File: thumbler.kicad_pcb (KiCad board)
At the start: 2 copper layers, 255 parts, among them J1 USB_B_Micro, J2 Conn_01x04, J3 Conn_01x04, J4 DIN-5_180degree, J5 Conn_01x04, J6 DIN-5_180degree, J7 Conn_01x04, J8 USB_B_Micro, SW1 SW_Push, SW2 SW_DIP_x05, SW3 SW_Push, SW4 SW_DIP_x05, U1 STM32F072C8Tx, U2 MCP1700-3302E_SOT89, U3 MCP1700-3302E_SOT89, U4 STM32F072C8Tx, X1 ENCODER_ANO

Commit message: revised layout basically done, minus thumbs
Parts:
- removed D37, D38, D39, D40, D41, D42, D43, D44, D46, D47, D48, D49, D50, D56, D57, D58, D59, D60, D61, D62, D63, D64, D65, D67, D68, D69, D70, D71, D72, D73, D74, D75: 1N4148, Diode_THT:D_DO-35_SOD27_P7.62mm_Horizontal
- removed S36, S37, S38, S39, S40, S41, S42, S43, S47, S48, S49, S50, S51, S52, S53, S54, S55, S56, S57, S58, S59, S60, S61, S62, S63, S64, S65, S66, S67, S68, S69, S70: Kailh_Hotplug, keyswitches:Kailh_socket_MX_platemount
- added D36: 1N4148, Diode_THT:D_DO-35_SOD27_P7.62mm_Horizontal, F.Cu at (467.1, 256.4)
- added D36: 1N4148, Diode_THT:D_DO-35_SOD27_P7.62mm_Horizontal, F.Cu at (429.0, 246.9)
- added D36: 1N4148, Diode_THT:D_DO-35_SOD27_P7.62mm_Horizontal, F.Cu at (410.0, 236.9)
- added D36: 1N4148, Diode_THT:D_DO-35_SOD27_P7.62mm_Horizontal, F.Cu at (390.9, 234.9)
- added D36: 1N4148, Diode_THT:D_DO-35_SOD27_P7.62mm_Horizontal, F.Cu at (371.9, 238.9)
- added D36: 1N4148, Diode_THT:D_DO-35_SOD27_P7.62mm_Horizontal, F.Cu at (352.8, 242.9)
- added D36: 1N4148, Diode_THT:D_DO-35_SOD27_P7.62mm_Horizontal, F.Cu at (467.1, 208.8)
- added D36: 1N4148, Diode_THT:D_DO-35_SOD27_P7.62mm_Horizontal, F.Cu at (448.1, 208.8)
- added D36: 1N4148, Diode_THT:D_DO-35_SOD27_P7.62mm_Horizontal, F.Cu at (429.0, 227.8)
- added D36: 1N4148, Diode_THT:D_DO-35_SOD27_P7.62mm_Horizontal, F.Cu at (410.0, 217.8)
- added D36: 1N4148, Diode_THT:D_DO-35_SOD27_P7.62mm_Horizontal, F.Cu at (390.9, 215.8)
- added D36: 1N4148, Diode_THT:D_DO-35_SOD27_P7.62mm_Horizontal, F.Cu at (448.1, 246.9)
- added D36: 1N4148, Diode_THT:D_DO-35_SOD27_P7.62mm_Horizontal, F.Cu at (371.9, 219.8)
- added D36: 1N4148, Diode_THT:D_DO-35_SOD27_P7.62mm_Horizontal, F.Cu at (352.8, 223.8)
- added D36: 1N4148, Diode_THT:D_DO-35_SOD27_P7.62mm_Horizontal, F.Cu at (467.1, 189.7)
- added D36: 1N4148, Diode_THT:D_DO-35_SOD27_P7.62mm_Horizontal, F.Cu at (448.1, 189.7)
- added D36: 1N4148, Diode_THT:D_DO-35_SOD27_P7.62mm_Horizontal, F.Cu at (429.0, 208.8)
- added D36: 1N4148, Diode_THT:D_DO-35_SOD27_P7.62mm_Horizontal, F.Cu at (410.0, 198.8)
- added D36: 1N4148, Diode_THT:D_DO-35_SOD27_P7.62mm_Horizontal, F.Cu at (390.9, 196.8)
- added D36: 1N4148, Diode_THT:D_DO-35_SOD27_P7.62mm_Horizontal, F.Cu at (371.9, 200.8)
- added D36: 1N4148, Diode_THT:D_DO-35_SOD27_P7.62mm_Horizontal, F.Cu at (352.8, 204.8)
- added D36: 1N4148, Diode_THT:D_DO-35_SOD27_P7.62mm_Horizontal, F.Cu at (467.1, 170.7)
- added D36: 1N4148, Diode_THT:D_DO-35_SOD27_P7.62mm_Horizontal, F.Cu at (429.0, 265.9)
- added D36: 1N4148, Diode_THT:D_DO-35_SOD27_P7.62mm_Horizontal, F.Cu at (438.5, 170.7)
- added D36: 1N4148, Diode_THT:D_DO-35_SOD27_P7.62mm_Horizontal, F.Cu at (429.0, 189.7)
- added D36: 1N4148, Diode_THT:D_DO-35_SOD27_P7.62mm_Horizontal, F.Cu at (410.0, 179.7)
- added D36: 1N4148, Diode_THT:D_DO-35_SOD27_P7.62mm_Horizontal, F.Cu at (390.9, 177.7)
- added D36: 1N4148, Diode_THT:D_DO-35_SOD27_P7.62mm_Horizontal, F.Cu at (371.9, 181.7)
- added D36: 1N4148, Diode_THT:D_DO-35_SOD27_P7.62mm_Horizontal, F.Cu at (410.0, 255.9)
- added D36: 1N4148, Diode_THT:D_DO-35_SOD27_P7.62mm_Horizontal, F.Cu at (390.9, 253.9)
- added D36: 1N4148, Diode_THT:D_DO-35_SOD27_P7.62mm_Horizontal, F.Cu at (371.9, 257.9)
- added D36: 1N4148, Diode_THT:D_DO-35_SOD27_P7.62mm_Horizontal, F.Cu at (352.8, 261.9)
- added D36: 1N4148, Diode_THT:D_DO-35_SOD27_P7.62mm_Horizontal, F.Cu at (467.1, 227.8)
- added D36: 1N4148, Diode_THT:D_DO-35_SOD27_P7.62mm_Horizontal, F.Cu at (448.1, 227.8)
- added S35: Kailh_Hotplug, keyswitches:Kailh_socket_MX_platemount, F.Cu at (476.0, 248.3)
- added S35: Kailh_Hotplug, keyswitches:Kailh_socket_MX_platemount, F.Cu at (437.9, 238.8)
- added S35: Kailh_Hotplug, keyswitches:Kailh_socket_MX_platemount, F.Cu at (418.9, 228.8)
- added S35: Kailh_Hotplug, keyswitches:Kailh_socket_MX_platemount, F.Cu at (399.8, 226.8)
- added S35: Kailh_Hotplug, keyswitches:Kailh_socket_MX_platemount, F.Cu at (380.8, 230.8)
- added S35: Kailh_Hotplug, keyswitches:Kailh_socket_MX_platemount, F.Cu at (361.7, 234.8)
- added S35: Kailh_Hotplug, keyswitches:Kailh_socket_MX_platemount, F.Cu at (476.0, 200.7)
- added S35: Kailh_Hotplug, keyswitches:Kailh_socket_MX_platemount, F.Cu at (457.0, 200.7)
- added S35: Kailh_Hotplug, keyswitches:Kailh_socket_MX_platemount, F.Cu at (437.9, 219.7)
- added S35: Kailh_Hotplug, keyswitches:Kailh_socket_MX_platemount, F.Cu at (418.9, 209.7)
- added S35: Kailh_Hotplug, keyswitches:Kailh_socket_MX_platemount, F.Cu at (399.8, 207.7)
- added S35: Kailh_Hotplug, keyswitches:Kailh_socket_MX_platemount, F.Cu at (457.0, 238.8)
- added S35: Kailh_Hotplug, keyswitches:Kailh_socket_MX_platemount, F.Cu at (380.8, 211.7)
- added S35: Kailh_Hotplug, keyswitches:Kailh_socket_MX_platemount, F.Cu at (361.7, 215.7)
- added S35: Kailh_Hotplug, keyswitches:Kailh_socket_MX_platemount, F.Cu at (476.0, 181.6)
- added S35: Kailh_Hotplug, keyswitches:Kailh_socket_MX_platemount, F.Cu at (457.0, 181.6)
- added S35: Kailh_Hotplug, keyswitches:Kailh_socket_MX_platemount, F.Cu at (437.9, 200.7)
- added S35: Kailh_Hotplug, keyswitches:Kailh_socket_MX_platemount, F.Cu at (418.9, 190.7)
- added S35: Kailh_Hotplug, keyswitches:Kailh_socket_MX_platemount, F.Cu at (399.8, 188.7)
- added S35: Kailh_Hotplug, keyswitches:Kailh_socket_MX_platemount, F.Cu at (380.8, 192.7)
- added S35: Kailh_Hotplug, keyswitches:Kailh_socket_MX_platemount, F.Cu at (361.7, 196.7)
- added S35: Kailh_Hotplug, keyswitches:Kailh_socket_MX_platemount, F.Cu at (476.0, 162.6)
- added S35: Kailh_Hotplug, keyswitches:Kailh_socket_MX_platemount, F.Cu at (437.9, 257.8)
- added S35: Kailh_Hotplug, keyswitches:Kailh_socket_MX_platemount, F.Cu at (447.5, 162.6)
- added S35: Kailh_Hotplug, keyswitches:Kailh_socket_MX_platemount, F.Cu at (437.9, 181.6)
- added S35: Kailh_Hotplug, keyswitches:Kailh_socket_MX_platemount, F.Cu at (418.9, 171.6)
- added S35: Kailh_Hotplug, keyswitches:Kailh_socket_MX_platemount, F.Cu at (399.8, 169.6)
- added S35: Kailh_Hotplug, keyswitches:Kailh_socket_MX_platemount, F.Cu at (380.8, 173.6)
- added S35: Kailh_Hotplug, keyswitches:Kailh_socket_MX_platemount, F.Cu at (418.9, 247.8)
- added S35: Kailh_Hotplug, keyswitches:Kailh_socket_MX_platemount, F.Cu at (399.8, 245.8)
- added S35: Kailh_Hotplug, keyswitches:Kailh_socket_MX_platemount, F.Cu at (380.8, 249.8)
- added S35: Kailh_Hotplug, keyswitches:Kailh_socket_MX_platemount, F.Cu at (361.7, 253.8)
- added S35: Kailh_Hotplug, keyswitches:Kailh_socket_MX_platemount, F.Cu at (476.0, 219.7)
- added S35: Kailh_Hotplug, keyswitches:Kailh_socket_MX_platemount, F.Cu at (457.0, 219.7)
- moved TP23 256.2 mm to (328.2, 219.9)
- moved TP26 256.2 mm to (328.3, 212.7)
- moved TP28 256.2 mm to (305.9, 200.7)
- moved TP30 256.2 mm to (313.6, 200.9)
- moved TP33 256.2 mm to (337.1, 212.1)
- moved TP36 256.2 mm to (321.5, 218.4)
- moved TP38 256.2 mm to (305.9, 214.4)
- moved TP24 256.2 mm to (328.0, 205.8)
- moved TP25 256.2 mm to (313.7, 211.4)
- moved TP31 256.2 mm to (336.3, 218.8)
- moved TP34 256.2 mm to (337.8, 205.6)
- moved TP35 256.2 mm to (319.9, 205.6)
- moved TP37 256.2 mm to (322.9, 200.6)
- moved TP27 256.2 mm to (317.8, 211.9)
- moved TP29 256.2 mm to (298.2, 219.0)
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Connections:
- D10 pad 1: L_ROW1 -> L_ROW2
- D10 pad 2: Net-(D6-Pad2) -> Net-(D10-Pad2)
- D11 pad 1: L_ROW1 -> L_ROW3
- D11 pad 2: Net-(D6-Pad2) -> Net-(D11-Pad2)
- D12 pad 1: L_ROW1 -> L_ROW4
- D12 pad 2: Net-(D6-Pad2) -> Net-(D12-Pad2)
- D13 pad 1: L_ROW1 -> L_ROW5
- D13 pad 2: Net-(D6-Pad2) -> Net-(D13-Pad2)
- D14 pad 2: Net-(D6-Pad2) -> Net-(D14-Pad2)
- D15 pad 1: L_ROW1 -> L_ROW2
- D15 pad 2: Net-(D6-Pad2) -> Net-(D15-Pad2)
- D16 pad 1: L_ROW1 -> L_ROW3
- D16 pad 2: Net-(D6-Pad2) -> Net-(D16-Pad2)
- D17 pad 1: L_ROW1 -> L_ROW4
- D17 pad 2: Net-(D6-Pad2) -> Net-(D17-Pad2)
- D18 pad 1: L_ROW1 -> L_ROW5
- D18 pad 2: Net-(D6-Pad2) -> Net-(D18-Pad2)
- D19 pad 2: Net-(D6-Pad2) -> Net-(D19-Pad2)
- D20 pad 1: L_ROW1 -> L_ROW2
- D20 pad 2: Net-(D6-Pad2) -> Net-(D20-Pad2)
- D21 pad 1: L_ROW1 -> L_ROW3
- D21 pad 2: Net-(D6-Pad2) -> Net-(D21-Pad2)
- D22 pad 1: L_ROW1 -> L_ROW4
- D22 pad 2: Net-(D6-Pad2) -> Net-(D22-Pad2)
- D23 pad 1: L_ROW1 -> L_ROW5
- D23 pad 2: Net-(D6-Pad2) -> Net-(D23-Pad2)
- D24 pad 2: Net-(D6-Pad2) -> Net-(D24-Pad2)
- D25 pad 1: L_ROW1 -> L_ROW2
- D25 pad 2: Net-(D6-Pad2) -> Net-(D25-Pad2)
- D26 pad 1: L_ROW1 -> L_ROW3
- D26 pad 2: Net-(D6-Pad2) -> Net-(D26-Pad2)
- D27 pad 1: L_ROW1 -> L_ROW4
- D27 pad 2: Net-(D6-Pad2) -> Net-(D27-Pad2)
- D28 pad 1: L_ROW1 -> L_ROW5
- D28 pad 2: Net-(D6-Pad2) -> Net-(D28-Pad2)
- D3 pad 1: L_ROW4 -> L_ROW5
- D32 pad 1: L_ROW1 -> L_ROW2
- D32 pad 2: Net-(D6-Pad2) -> Net-(D32-Pad2)
- D33 pad 1: L_ROW1 -> L_ROW3
- D33 pad 2: Net-(D6-Pad2) -> Net-(D33-Pad2)
- D34 pad 1: L_ROW1 -> L_ROW4
- D34 pad 2: Net-(D6-Pad2) -> Net-(D34-Pad2)
- D35 pad 1: L_ROW1 -> L_ROW5
- D35 pad 2: Net-(D6-Pad2) -> Net-(D35-Pad2)
- D4 pad 1: L_ROW1 -> L_ROW3
- D4 pad 2: Net-(D6-Pad2) -> Net-(D4-Pad2)
- D5 pad 1: L_ROW1 -> L_ROW4
- D5 pad 2: Net-(D6-Pad2) -> Net-(D5-Pad2)
- D7 pad 1: L_ROW1 -> L_ROW2
- D7 pad 2: Net-(D6-Pad2) -> Net-(D7-Pad2)
- D8 pad 1: L_ROW1 -> L_ROW5
- D8 pad 2: Net-(D6-Pad2) -> Net-(D8-Pad2)
- D9 pad 2: Net-(D6-Pad2) -> Net-(D9-Pad2)
- S10 pad 1: Net-(D6-Pad2) -> Net-(D12-Pad2)
- S10 pad 2: Net-(R5-Pad2) -> Net-(R6-Pad2)
- S11 pad 1: Net-(D6-Pad2) -> Net-(D13-Pad2)
- S11 pad 2: Net-(R5-Pad2) -> Net-(R6-Pad2)
- S12 pad 1: Net-(D6-Pad2) -> Net-(D14-Pad2)
- S12 pad 2: Net-(R5-Pad2) -> Net-(R8-Pad2)
- S13 pad 1: Net-(D6-Pad2) -> Net-(D15-Pad2)
- S13 pad 2: Net-(R5-Pad2) -> Net-(R8-Pad2)
- S14 pad 1: Net-(D6-Pad2) -> Net-(D16-Pad2)
- S14 pad 2: Net-(R5-Pad2) -> Net-(R8-Pad2)
- S15 pad 1: Net-(D6-Pad2) -> Net-(D17-Pad2)
- S15 pad 2: Net-(R5-Pad2) -> Net-(R8-Pad2)
- S16 pad 1: Net-(D6-Pad2) -> Net-(D18-Pad2)
- S16 pad 2: Net-(R5-Pad2) -> Net-(R8-Pad2)
- S17 pad 1: Net-(D6-Pad2) -> Net-(D19-Pad2)
- S17 pad 2: Net-(R5-Pad2) -> Net-(R9-Pad2)
- S18 pad 1: Net-(D6-Pad2) -> Net-(D20-Pad2)
- S18 pad 2: Net-(R5-Pad2) -> Net-(R9-Pad2)
- S19 pad 1: Net-(D6-Pad2) -> Net-(D21-Pad2)
- S19 pad 2: Net-(R5-Pad2) -> Net-(R9-Pad2)
- S2 pad 1: Net-(D6-Pad2) -> Net-(D4-Pad2)
- S2 pad 2: Net-(R5-Pad2) -> Net-(R3-Pad2)
- S20 pad 1: Net-(D6-Pad2) -> Net-(D22-Pad2)
- S20 pad 2: Net-(R5-Pad2) -> Net-(R9-Pad2)
- S21 pad 1: Net-(D6-Pad2) -> Net-(D23-Pad2)
- S21 pad 2: Net-(R5-Pad2) -> Net-(R9-Pad2)
- S22 pad 1: Net-(D6-Pad2) -> Net-(D24-Pad2)
- S22 pad 2: Net-(R5-Pad2) -> Net-(R10-Pad2)
- S23 pad 1: Net-(D6-Pad2) -> Net-(D25-Pad2)
- S23 pad 2: Net-(R5-Pad2) -> Net-(R10-Pad2)
- S24 pad 1: Net-(D6-Pad2) -> Net-(D26-Pad2)
- S24 pad 2: Net-(R5-Pad2) -> Net-(R10-Pad2)
- S25 pad 1: Net-(D6-Pad2) -> Net-(D27-Pad2)
- S25 pad 2: Net-(R5-Pad2) -> Net-(R10-Pad2)
- S26 pad 1: Net-(D6-Pad2) -> Net-(D28-Pad2)
- S26 pad 2: Net-(R5-Pad2) -> Net-(R10-Pad2)
- S3 pad 1: Net-(D6-Pad2) -> Net-(D5-Pad2)
- S3 pad 2: Net-(R5-Pad2) -> Net-(R3-Pad2)
- S30 pad 1: Net-(D6-Pad2) -> Net-(D32-Pad2)
- S30 pad 2: Net-(R5-Pad2) -> Net-(R12-Pad2)
- S31 pad 1: Net-(D6-Pad2) -> Net-(D33-Pad2)
- S31 pad 2: Net-(R5-Pad2) -> Net-(R12-Pad2)
- S32 pad 1: Net-(D6-Pad2) -> Net-(D34-Pad2)
- S32 pad 2: Net-(R5-Pad2) -> Net-(R12-Pad2)
- S33 pad 1: Net-(D6-Pad2) -> Net-(D35-Pad2)
- S33 pad 2: Net-(R5-Pad2) -> Net-(R12-Pad2)
- S5 pad 1: Net-(D6-Pad2) -> Net-(D7-Pad2)
- S6 pad 1: Net-(D6-Pad2) -> Net-(D8-Pad2)
- S7 pad 1: Net-(D6-Pad2) -> Net-(D9-Pad2)
- S7 pad 2: Net-(R5-Pad2) -> Net-(R6-Pad2)
- S8 pad 1: Net-(D6-Pad2) -> Net-(D10-Pad2)
- S8 pad 2: Net-(R5-Pad2) -> Net-(R6-Pad2)
- S9 pad 1: Net-(D6-Pad2) -> Net-(D11-Pad2)
- S9 pad 2: Net-(R5-Pad2) -> Net-(R6-Pad2)
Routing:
- net Net-(D36-Pad2): track 3.58 -> 125.2 mm
- net Net-(D6-Pad2): track 100.9 -> 3.48 mm
- net Net-(D69-Pad2): track 3.86 -> 0.00 mm
- net Net-(D39-Pad2): track 3.79 -> 0.00 mm
- net Net-(D49-Pad2): track 3.78 -> 0.00 mm
- net Net-(D60-Pad2): track 3.77 -> 0.00 mm
- net Net-(D41-Pad2): track 3.74 -> 0.00 mm
- net Net-(D47-Pad2): track 3.74 -> 0.00 mm
- net Net-(D65-Pad2): track 3.71 -> 0.00 mm
- net Net-(D67-Pad2): track 3.71 -> 0.00 mm
- net Net-(D44-Pad2): track 3.70 -> 0.00 mm
- net Net-(D68-Pad2): track 3.69 -> 0.00 mm
- net Net-(D46-Pad2): track 3.69 -> 0.00 mm
- net Net-(D73-Pad2): track 3.67 -> 0.00 mm
- net Net-(D59-Pad2): track 3.65 -> 0.00 mm
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
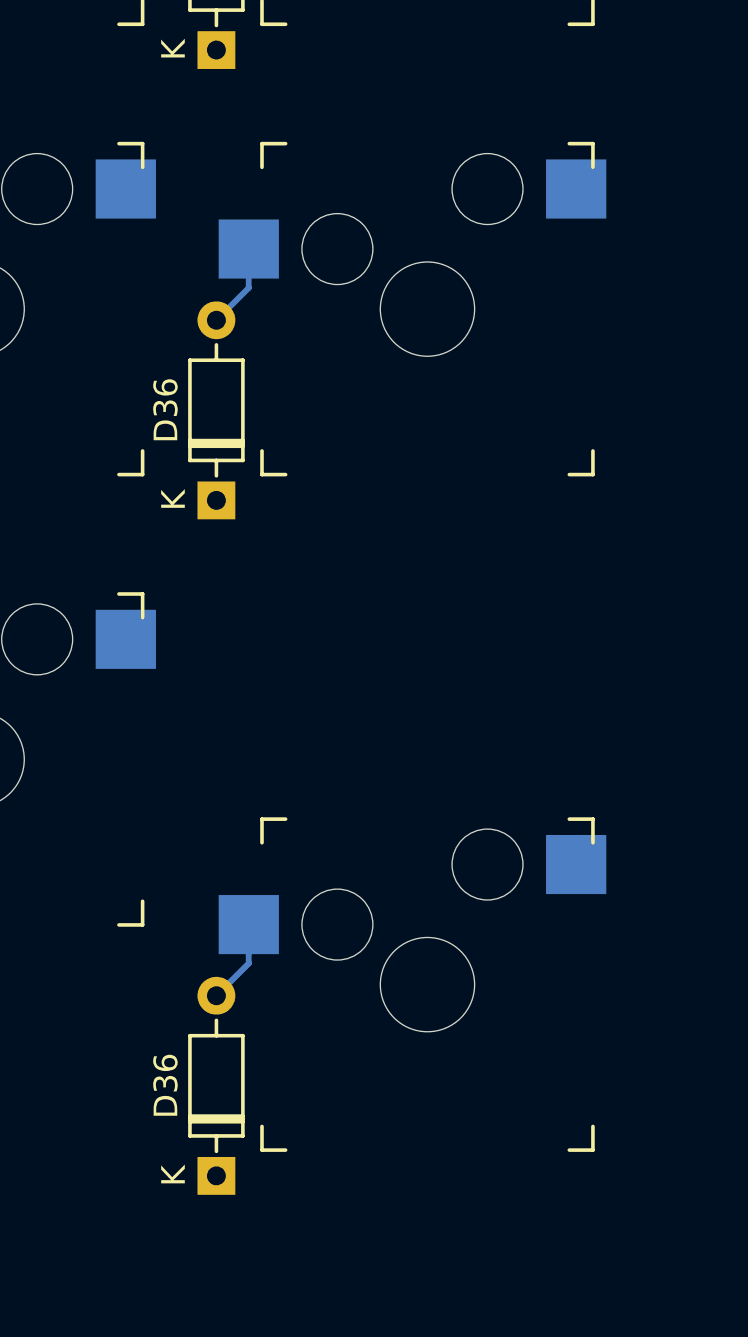
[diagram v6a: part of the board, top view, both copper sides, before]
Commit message: fix right enter placement; still need to reannotate
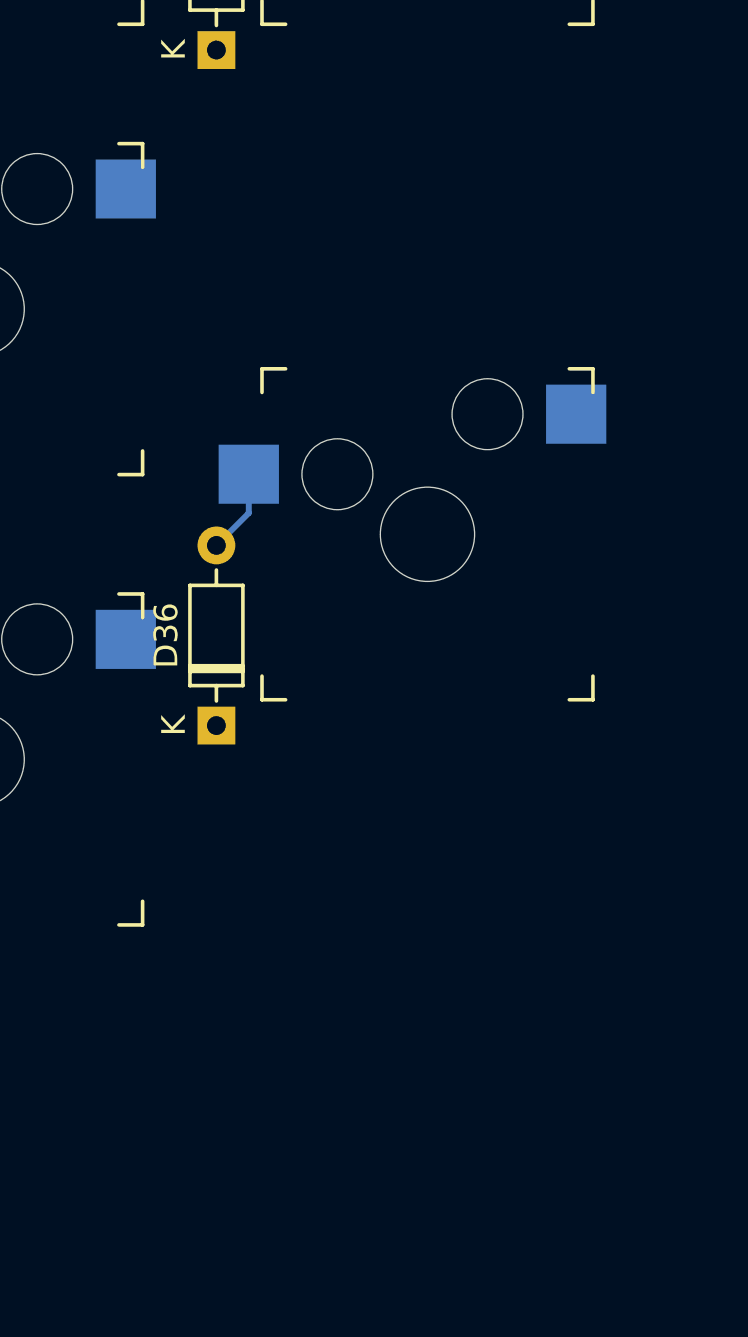
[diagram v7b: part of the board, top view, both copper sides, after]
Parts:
- removed the D36 at (467.1, 256.4)
- removed the S35 at (476.0, 248.3)
- moved S35 9.53 mm to (476.0, 229.2)
- moved D36 9.52 mm to (467.1, 237.3)
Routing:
- net Net-(D36-Pad2): track 125.2 -> 121.6 mm

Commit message: minor tidying
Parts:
- moved J4 50.9 mm to (255.6, 144.7)
- moved JP1 50.9 mm to (234.5, 144.7)
- moved J6 50.1 mm to (313.3, 145.5)
- moved SW3 22.4 mm to (361.9, 131.5)
- moved C13 22.4 mm to (353.2, 130.5)
- moved D45 22.4 mm to (443.2, 130.6)
- moved C14 22.4 mm to (463.0, 129.9)
- moved C15 22.4 mm to (468.4, 140.9)
- moved C16 22.4 mm to (417.3, 140.8)
- moved C18 22.4 mm to (417.3, 139.3)
- moved C20 22.4 mm to (407.6, 130.3)
- moved D76 22.4 mm to (458.3, 135.6)
- moved J5 22.4 mm to (383.7, 135.2)
- moved J7 22.4 mm to (383.6, 126.5)
- moved R17 22.4 mm to (438.3, 136.1)
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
